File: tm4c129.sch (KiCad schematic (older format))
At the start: 45 parts, among them SW401 RST_SW, U401 TM4C1294NCPDTGOOD, Y401 Crystal_GND24, Y402 Crystal

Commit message: replaced battery with ldo connected to external vbatt. Layout passes DRC
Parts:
- removed BT401: Battery_Cell, Battery:BatteryHolder_Keystone_1058_1x2032, symbol Device:Battery_Cell
- added C1: 0.1u, Capacitor_SMD:C_0603_1608Metric, symbol Device:C_Small
- added C2: 10u, Capacitor_SMD:C_0603_1608Metric, symbol Device:C_Small
- added R1: 0, Capacitor_SMD:C_0603_1608Metric, symbol Device:R_Small
- added R2: DNP, Capacitor_SMD:C_0603_1608Metric, symbol Device:R_Small
- added U1: LT1761-3, Package_TO_SOT_SMD:TSOT-23-5, symbol Regulator_Linear:LT1761-3
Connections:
- net labels added: +BATT, VBat_R
- wire segments 249 -> 261
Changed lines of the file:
@@
 	5900 900  5900 1050
-$Comp
-L Device:Battery_Cell BT401
-U 1 1 5D11D2E9
-P 1450 1300
-F 0 "BT401" H 1568 1396 50  0000 L CNN
-F 1 "Battery_Cell" H 1568 1305 50  0000 L CNN
-F 2 "Battery:BatteryHolder_Keystone_1058_1x2032" V 1450 1360 50  0001 C CNN
-F 3 "~" V 1450 1360 50  0001 C CNN
-	1    1450 1300
-	1    0    0    -1
-$EndComp
-Wire Wire Line
-	1450 1100 1450 1050
-Wire Wire Line
-	1450 1050 1850 1050
 $Comp
 L Device:R_Small R401
@@
 Wire Wire Line
 	2150 1050 2150 1150
-Text Label 2400 1050 0    50   ~ 0
-VBat
+Text Label 2550 1050 0    50   ~ 0
+VBat_R
 Text Label 1450 1050 0    50   ~ 0
 Batt_Pos
@@
 L power:GND #PWR0405
 U 1 1 5D116091
-P 1450 1500
-F 0 "#PWR0405" H 1450 1250 50  0001 C CNN
-F 1 "GND" H 1455 1327 50  0000 C CNN
-F 2 "" H 1450 1500 50  0001 C CNN
-F 3 "" H 1450 1500 50  0001 C CNN
-	1    1450 1500
+P 2150 1500
+F 0 "#PWR0405" H 2150 1250 50  0001 C CNN
+F 1 "GND" H 2155 1327 50  0000 C CNN
+F 2 "" H 2150 1500 50  0001 C CNN
+F 3 "" H 2150 1500 50  0001 C CNN
+	1    2150 1500
 	1    0    0    -1
 $EndComp
@@
 $EndComp
 Wire Wire Line
-	1450 1400 1450 1450
-Wire Wire Line
-	1450 1450 2150 1450
-Wire Wire Line
-	2150 1450 2150 1350
-Wire Wire Line
-	1450 1500 1450 1450
-Connection ~ 1450 1450
-Wire Wire Line
 	5900 1150 5900 1300
-Wire Wire Line
-	2750 1050 2150 1050
-Connection ~ 2150 1050
 $Comp
 L Device:R_Small R407
@@
 Wire Wire Line
 	2600 2600 2600 2650
+Connection ~ 2600 2650
+Wire Wire Line
+	2450 2550 2450 2850
+Wire Wire Line
+	2150 1350 2150 1500
+$Comp
+L Regulator_Linear:LT1761-3 U1
+U 1 1 5D319EB9
+P 1050 1150
+F 0 "U1" H 1050 1517 50  0000 C CNN
+F 1 "LT1761-3" H 1050 1426 50  0000 C CNN
+F 2 "Package_TO_SOT_SMD:TSOT-23-5" H 1050 1475 50  0001 C CNN
+F 3 "https://www.analog.com/media/en/technical-documentation/data-sheets/1761sff.pdf" H 1050 1150 50  0001 C CNN
+	1    1050 1150
+	1    0    0    -1
+$EndComp
+Wire Wire Line
+	650  1050 600  1050
+Wire Wire Line
+	600  1050 600  1150
+Wire Wire Line
+	600  1150 650  1150
+Wire Wire Line
+	600  1050 600  950
+Connection ~ 600  1050
+$Comp
+L power:+BATT #PWR0101
+U 1 1 5D39C749
+P 600 950
+F 0 "#PWR0101" H 600 800 50  0001 C CNN
+F 1 "+BATT" H 615 1123 50  0000 C CNN
+F 2 "" H 600 950 50  0001 C CNN
+F 3 "" H 600 950 50  0001 C CNN
+	1    600  950
+	1    0    0    -1
+$EndComp
+Wire Wire Line
+	1050 1450 1050 1500
+$Comp
+L power:GND #PWR0102
+U 1 1 5D3B002F
+P 1050 1500
+F 0 "#PWR0102" H 1050 1250 50  0001 C CNN
+F 1 "GND" H 1055 1327 50  0000 C CNN
+F 2 "" H 1050 1500 50  0001 C CNN
+F 3 "" H 1050 1500 50  0001 C CNN
+	1    1050 1500
+	1    0    0    -1
+$EndComp
+$Comp
+L Device:C_Small C2
+U 1 1 5D3B0A26
+P 1800 1150
+F 0 "C2" H 1892 1196 50  0000 L CNN
+F 1 "10u" H 1892 1105 50  0000 L CNN
+F 2 "Capacitor_SMD:C_0603_1608Metric" H 1800 1150 50  0001 C CNN
+F 3 "~" H 1800 1150 50  0001 C CNN
+	1    1800 1150
+	1    0    0    -1
+$EndComp
+Wire Wire Line
+	1800 1250 1800 1300
+$Comp
+L power:GND #PWR0103
+U 1 1 5D3C4347
+P 1800 1300
+F 0 "#PWR0103" H 1800 1050 50  0001 C CNN
+F 1 "GND" H 1805 1127 50  0000 C CNN
+F 2 "" H 1800 1300 50  0001 C CNN
+F 3 "" H 1800 1300 50  0001 C CNN
+	1    1800 1300
+	1    0    0    -1
+$EndComp
+$Comp
+L Device:C_Small C1
+U 1 1 5D3E9FEA
+P 1600 1150
+F 0 "C1" H 1692 1196 50  0000 L CNN
+F 1 "0.1u" H 1692 1105 50  0000 L CNN
+F 2 "Capacitor_SMD:C_0603_1608Metric" H 1600 1150 50  0001 C CNN
+F 3 "~" H 1600 1150 50  0001 C CNN
+	1    1600 1150
+	1    0    0    -1
+$EndComp
+Connection ~ 1800 1050
+Wire Wire Line
+	1800 1050 1850 1050
+Wire Wire Line
+	1450 1050 1600 1050
+Connection ~ 1600 1050
+Wire Wire Line
+	1600 1050 1800 1050
+Wire Wire Line
+	1450 1150 1500 1150
+Wire Wire Line
+	1500 1300 1600 1300
+Wire Wire Line
+	1600 1300 1600 1250
+Wire Wire Line
+	1500 1150 1500 1300
+$Comp
+L Device:R_Small R1
+U 1 1 5D4424D9
+P 2300 1050
+F 0 "R1" V 2104 1050 50  0000 C CNN
+F 1 "0" V 2195 1050 50  0000 C CNN
+F 2 "Capacitor_SMD:C_0603_1608Metric" H 2300 1050 50  0001 C CNN
+F 3 "~" H 2300 1050 50  0001 C CNN
+	1    2300 1050
+	0    1    1    0
+$EndComp
+Text Label 2100 1050 0    50   ~ 0
+VBat
+Wire Wire Line
+	2200 1050 2150 1050
+Connection ~ 2150 1050
+Wire Wire Line
+	2400 1050 2500 1050
+$Comp
+L Device:R_Small R2
+U 1 1 5D4934F5
+P 2500 900
+F 0 "R2" H 2441 854 50  0000 R CNN
+F 1 "DNP" H 2441 945 50  0000 R CNN
+F 2 "Capacitor_SMD:C_0603_1608Metric" H 2500 900 50  0001 C CNN
+F 3 "~" H 2500 900 50  0001 C CNN
+	1    2500 900
+	-1   0    0    1
+$EndComp
+Wire Wire Line
+	2500 1000 2500 1050
+Connection ~ 2500 1050
+Wire Wire Line
+	2500 1050 2750 1050
+$Comp
+L power:+3.3V #PWR0104
+U 1 1 5D4A8C01
+P 2500 750
+F 0 "#PWR0104" H 2500 600 50  0001 C CNN
+F 1 "+3.3V" H 2515 923 50  0000 C CNN
+F 2 "" H 2500 750 50  0001 C CNN
+F 3 "" H 2500 750 50  0001 C CNN
+	1    2500 750
+	1    0    0    -1
+$EndComp
+Wire Wire Line
+	2500 750  2500 800
 Wire Bus Line
 	1700 4850 1700 7600
 Wire Bus Line
 	6000 2200 6000 7600
-Connection ~ 2600 2650
-Wire Wire Line
-	2450 2550 2450 2850
 $EndSCHEMATC

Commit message: moved ldo vbatt circuit to a sheet
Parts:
- removed C1: 0.1u, Capacitor_SMD:C_0603_1608Metric, symbol Device:C_Small
- removed C2: 10u, Capacitor_SMD:C_0603_1608Metric, symbol Device:C_Small
- removed R401: 51, Resistor_SMD:R_0603_1608Metric, symbol Device:R_Small
- removed U1: LT1761-3, Package_TO_SOT_SMD:TSOT-23-5, symbol Regulator_Linear:LT1761-3
- added R3: 51, Resistor_SMD:R_0603_1608Metric, symbol Device:R_Small
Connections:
- net labels removed: +BATT, Batt_Pos
- wire segments 261 -> 249
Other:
- moved on the sheet: C410, R1, R2
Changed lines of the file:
@@
 $Descr A4 11693 8268
 encoding utf-8
-Sheet 4 5
+Sheet 4 6
 Title "TM4C129"
 Date "2019-06-22"
@@
 	5900 900  5900 1050
 $Comp
-L Device:R_Small R401
-U 1 1 5D132E60
-P 1950 1050
-F 0 "R401" V 1754 1050 50  0000 C CNN
-F 1 "51" V 1845 1050 50  0000 C CNN
-F 2 "Resistor_SMD:R_0603_1608Metric" H 1950 1050 50  0001 C CNN
-F 3 "~" H 1950 1050 50  0001 C CNN
-	1    1950 1050
-	0    1    1    0
-$EndComp
-$Comp
 L Device:C_Small C410
 U 1 1 5D1335F6
-P 2150 1250
-F 0 "C410" H 2242 1296 50  0000 L CNN
-F 1 "0.1u" H 2242 1205 50  0000 L CNN
-F 2 "Capacitor_SMD:C_0603_1608Metric" H 2150 1250 50  0001 C CNN
-F 3 "~" H 2150 1250 50  0001 C CNN
-	1    2150 1250
-	1    0    0    -1
-$EndComp
-Wire Wire Line
-	2050 1050 2150 1050
-Wire Wire Line
-	2150 1050 2150 1150
-Text Label 2550 1050 0    50   ~ 0
+P 1650 1250
+F 0 "C410" H 1742 1296 50  0000 L CNN
+F 1 "0.1u" H 1742 1205 50  0000 L CNN
+F 2 "Capacitor_SMD:C_0603_1608Metric" H 1650 1250 50  0001 C CNN
+F 3 "~" H 1650 1250 50  0001 C CNN
+	1    1650 1250
+	1    0    0    -1
+$EndComp
+Wire Wire Line
+	1550 1050 1650 1050
+Wire Wire Line
+	1650 1050 1650 1150
+Text Label 2150 1050 0    50   ~ 0
 VBat_R
-Text Label 1450 1050 0    50   ~ 0
-Batt_Pos
 $Comp
 L Device:Crystal Y402
@@
 L power:GND #PWR0405
 U 1 1 5D116091
-P 2150 1500
-F 0 "#PWR0405" H 2150 1250 50  0001 C CNN
-F 1 "GND" H 2155 1327 50  0000 C CNN
-F 2 "" H 2150 1500 50  0001 C CNN
-F 3 "" H 2150 1500 50  0001 C CNN
-	1    2150 1500
+P 1650 1500
+F 0 "#PWR0405" H 1650 1250 50  0001 C CNN
+F 1 "GND" H 1655 1327 50  0000 C CNN
+F 2 "" H 1650 1500 50  0001 C CNN
+F 3 "" H 1650 1500 50  0001 C CNN
+	1    1650 1500
 	1    0    0    -1
 $EndComp
@@
 Text Notes 9500 650  0    50   ~ 0
 Bulk Cap should total 2.2uF to 22uF
-Text Notes 1050 800  0    50   ~ 0
-RC time circuit to meet ontime requirements
 Wire Bus Line
 	1700 4850 1550 4850
@@
 	2450 2550 2450 2850
 Wire Wire Line
-	2150 1350 2150 1500
-$Comp
-L Regulator_Linear:LT1761-3 U1
-U 1 1 5D319EB9
-P 1050 1150
-F 0 "U1" H 1050 1517 50  0000 C CNN
-F 1 "LT1761-3" H 1050 1426 50  0000 C CNN
-F 2 "Package_TO_SOT_SMD:TSOT-23-5" H 1050 1475 50  0001 C CNN
-F 3 "https://www.analog.com/media/en/technical-documentation/data-sheets/1761sff.pdf" H 1050 1150 50  0001 C CNN
-	1    1050 1150
-	1    0    0    -1
-$EndComp
-Wire Wire Line
-	650  1050 600  1050
-Wire Wire Line
-	600  1050 600  1150
-Wire Wire Line
-	600  1150 650  1150
-Wire Wire Line
-	600  1050 600  950
-Connection ~ 600  1050
-$Comp
-L power:+BATT #PWR0101
-U 1 1 5D39C749
-P 600 950
-F 0 "#PWR0101" H 600 800 50  0001 C CNN
-F 1 "+BATT" H 615 1123 50  0000 C CNN
-F 2 "" H 600 950 50  0001 C CNN
-F 3 "" H 600 950 50  0001 C CNN
-	1    600  950
-	1    0    0    -1
-$EndComp
-Wire Wire Line
-	1050 1450 1050 1500
-$Comp
-L power:GND #PWR0102
-U 1 1 5D3B002F
-P 1050 1500
-F 0 "#PWR0102" H 1050 1250 50  0001 C CNN
-F 1 "GND" H 1055 1327 50  0000 C CNN
-F 2 "" H 1050 1500 50  0001 C CNN
-F 3 "" H 1050 1500 50  0001 C CNN
-	1    1050 1500
-	1    0    0    -1
-$EndComp
-$Comp
-L Device:C_Small C2
-U 1 1 5D3B0A26
-P 1800 1150
-F 0 "C2" H 1892 1196 50  0000 L CNN
-F 1 "10u" H 1892 1105 50  0000 L CNN
-F 2 "Capacitor_SMD:C_0603_1608Metric" H 1800 1150 50  0001 C CNN
-F 3 "~" H 1800 1150 50  0001 C CNN
-	1    1800 1150
-	1    0    0    -1
-$EndComp
-Wire Wire Line
-	1800 1250 1800 1300
-$Comp
-L power:GND #PWR0103
-U 1 1 5D3C4347
-P 1800 1300
-F 0 "#PWR0103" H 1800 1050 50  0001 C CNN
-F 1 "GND" H 1805 1127 50  0000 C CNN
-F 2 "" H 1800 1300 50  0001 C CNN
-F 3 "" H 1800 1300 50  0001 C CNN
-	1    1800 1300
-	1    0    0    -1
-$EndComp
-$Comp
-L Device:C_Small C1
-U 1 1 5D3E9FEA
-P 1600 1150
-F 0 "C1" H 1692 1196 50  0000 L CNN
-F 1 "0.1u" H 1692 1105 50  0000 L CNN
-F 2 "Capacitor_SMD:C_0603_1608Metric" H 1600 1150 50  0001 C CNN
-F 3 "~" H 1600 1150 50  0001 C CNN
-	1    1600 1150
-	1    0    0    -1
-$EndComp
-Connection ~ 1800 1050
-Wire Wire Line
-	1800 1050 1850 1050
-Wire Wire Line
-	1450 1050 1600 1050
-Connection ~ 1600 1050
-Wire Wire Line
-	1600 1050 1800 1050
-Wire Wire Line
-	1450 1150 1500 1150
-Wire Wire Line
-	1500 1300 1600 1300
-Wire Wire Line
-	1600 1300 1600 1250
-Wire Wire Line
-	1500 1150 1500 1300
+	1650 1350 1650 1500
 $Comp
 L Device:R_Small R1
 U 1 1 5D4424D9
-P 2300 1050
-F 0 "R1" V 2104 1050 50  0000 C CNN
-F 1 "0" V 2195 1050 50  0000 C CNN
-F 2 "Capacitor_SMD:C_0603_1608Metric" H 2300 1050 50  0001 C CNN
-F 3 "~" H 2300 1050 50  0001 C CNN
-	1    2300 1050
+P 1900 1050
+F 0 "R1" V 1704 1050 50  0000 C CNN
+F 1 "0" V 1795 1050 50  0000 C CNN
+F 2 "Capacitor_SMD:C_0603_1608Metric" H 1900 1050 50  0001 C CNN
+F 3 "~" H 1900 1050 50  0001 C CNN
+	1    1900 1050
 	0    1    1    0
 $EndComp
-Text Label 2100 1050 0    50   ~ 0
+Text Label 1600 1050 0    50   ~ 0
 VBat
-Wire Wire Line
-	2200 1050 2150 1050
-Connection ~ 2150 1050
-Wire Wire Line
-	2400 1050 2500 1050
+Connection ~ 1650 1050
 $Comp
 L Device:R_Small R2
 U 1 1 5D4934F5
-P 2500 900
-F 0 "R2" H 2441 854 50  0000 R CNN
-F 1 "DNP" H 2441 945 50  0000 R CNN
-F 2 "Capacitor_SMD:C_0603_1608Metric" H 2500 900 50  0001 C CNN
-F 3 "~" H 2500 900 50  0001 C CNN
-	1    2500 900
+P 2550 850
+F 0 "R2" H 2491 804 50  0000 R CNN
+F 1 "DNP" H 2491 895 50  0000 R CNN
+F 2 "Capacitor_SMD:C_0603_1608Metric" H 2550 850 50  0001 C CNN
+F 3 "~" H 2550 850 50  0001 C CNN
+	1    2550 850
 	-1   0    0    1
 $EndComp
-Wire Wire Line
-	2500 1000 2500 1050
-Connection ~ 2500 1050
-Wire Wire Line
-	2500 1050 2750 1050
 $Comp
 L power:+3.3V #PWR0104
 U 1 1 5D4A8C01
-P 2500 750
-F 0 "#PWR0104" H 2500 600 50  0001 C CNN
-F 1 "+3.3V" H 2515 923 50  0000 C CNN
-F 2 "" H 2500 750 50  0001 C CNN
-F 3 "" H 2500 750 50  0001 C CNN
-	1    2500 750
-	1    0    0    -1
-$EndComp
-Wire Wire Line
-	2500 750  2500 800
+P 2550 700
+F 0 "#PWR0104" H 2550 550 50  0001 C CNN
+F 1 "+3.3V" H 2565 873 50  0000 C CNN
+F 2 "" H 2550 700 50  0001 C CNN
+F 3 "" H 2550 700 50  0001 C CNN
+	1    2550 700
+	1    0    0    -1
+$EndComp
+Wire Wire Line
+	2550 700  2550 750
+$Sheet
+S 700  950  550  200
+U 5D2CB049
+F0 "V_Batt" 50
+F1 "v_batt.sch" 50
+F2 "Vout" I R 1250 1050 50
+$EndSheet
+Text Notes 550  800  0    50   ~ 0
+RC time circuit to meet ontime requirements
+$Comp
+L Device:R_Small R3
+U 1 1 5D306A2C
+P 1450 1050
+AR Path="/5C80AE96/5D306A2C" Ref="R3"  Part="1"
+AR Path="/5C80AE96/5D2CB049/5D306A2C" Ref="R?"  Part="1"
+F 0 "R3" V 1254 1050 50  0000 C CNN
+F 1 "51" V 1345 1050 50  0000 C CNN
+F 2 "Resistor_SMD:R_0603_1608Metric" H 1450 1050 50  0001 C CNN
+F 3 "~" H 1450 1050 50  0001 C CNN
+	1    1450 1050
+	0    1    1    0
+$EndComp
+Wire Wire Line
+	1650 1050 1800 1050
+Wire Wire Line
+	1250 1050 1350 1050
+Wire Wire Line
+	2000 1050 2550 1050
+Wire Wire Line
+	2550 950  2550 1050
 Wire Bus Line
 	1700 4850 1700 7600
 Wire Bus Line
 	6000 2200 6000 7600
+Connection ~ 2550 1050
+Wire Wire Line
+	2550 1050 2750 1050
 $EndSCHEMATC

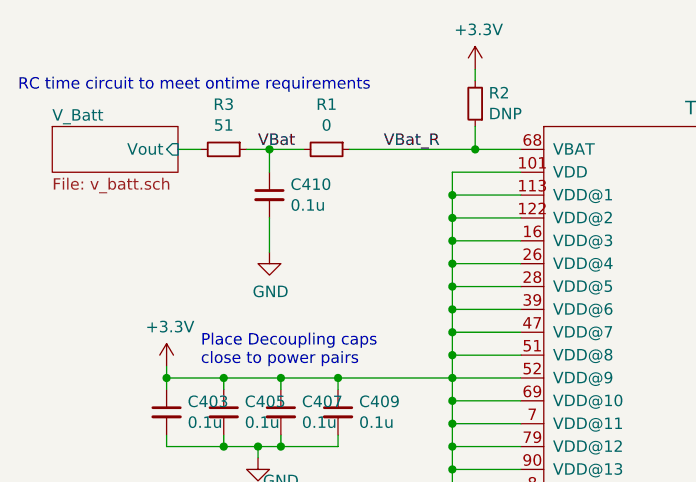
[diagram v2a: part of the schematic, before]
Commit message: removed rc filter on vbatt output. Included ltspice sim to prove it's unneeded.
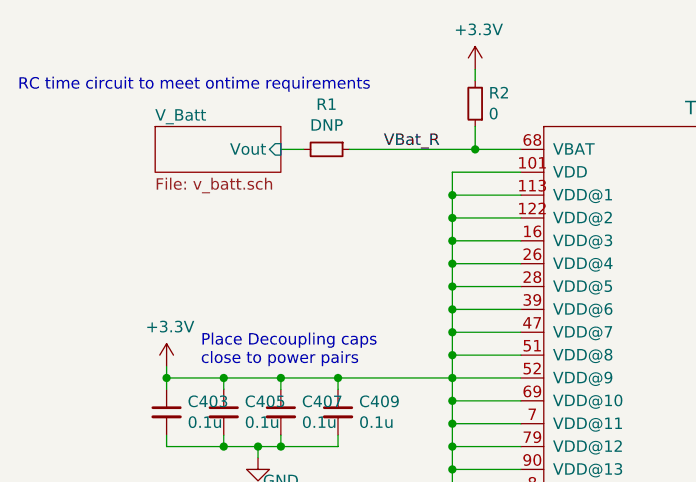
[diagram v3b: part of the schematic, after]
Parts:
- removed C410: 0.1u, Capacitor_SMD:C_0603_1608Metric, symbol Device:C_Small
- removed R3: 51, Resistor_SMD:R_0603_1608Metric, symbol Device:R_Small
- R1: value 0 -> DNP
- R2: value DNP -> 0
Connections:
- net labels removed: VBat
- wire segments 249 -> 245
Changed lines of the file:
@@
 Wire Wire Line
 	5900 900  5900 1050
-$Comp
-L Device:C_Small C410
-U 1 1 5D1335F6
-P 1650 1250
-F 0 "C410" H 1742 1296 50  0000 L CNN
-F 1 "0.1u" H 1742 1205 50  0000 L CNN
-F 2 "Capacitor_SMD:C_0603_1608Metric" H 1650 1250 50  0001 C CNN
-F 3 "~" H 1650 1250 50  0001 C CNN
-	1    1650 1250
-	1    0    0    -1
-$EndComp
-Wire Wire Line
-	1550 1050 1650 1050
-Wire Wire Line
-	1650 1050 1650 1150
 Text Label 2150 1050 0    50   ~ 0
 VBat_R
@@
 	1    6100 1100
 	0    1    -1   0
-$EndComp
-$Comp
-L power:GND #PWR0405
-U 1 1 5D116091
-P 1650 1500
-F 0 "#PWR0405" H 1650 1250 50  0001 C CNN
-F 1 "GND" H 1655 1327 50  0000 C CNN
-F 2 "" H 1650 1500 50  0001 C CNN
-F 3 "" H 1650 1500 50  0001 C CNN
-	1    1650 1500
-	1    0    0    -1
 $EndComp
 $Comp
@@
 Wire Wire Line
 	2450 2550 2450 2850
-Wire Wire Line
-	1650 1350 1650 1500
 $Comp
 L Device:R_Small R1
@@
 P 1900 1050
 F 0 "R1" V 1704 1050 50  0000 C CNN
-F 1 "0" V 1795 1050 50  0000 C CNN
+F 1 "DNP" V 1795 1050 50  0000 C CNN
 F 2 "Capacitor_SMD:C_0603_1608Metric" H 1900 1050 50  0001 C CNN
 F 3 "~" H 1900 1050 50  0001 C CNN
@@
 	0    1    1    0
 $EndComp
-Text Label 1600 1050 0    50   ~ 0
-VBat
-Connection ~ 1650 1050
 $Comp
 L Device:R_Small R2
@@
 P 2550 850
 F 0 "R2" H 2491 804 50  0000 R CNN
-F 1 "DNP" H 2491 895 50  0000 R CNN
+F 1 "0" H 2491 895 50  0000 R CNN
 F 2 "Capacitor_SMD:C_0603_1608Metric" H 2550 850 50  0001 C CNN
 F 3 "~" H 2550 850 50  0001 C CNN
@@
 	2550 700  2550 750
 $Sheet
-S 700  950  550  200
+S 1150 950  550  200
 U 5D2CB049
 F0 "V_Batt" 50
 F1 "v_batt.sch" 50
-F2 "Vout" I R 1250 1050 50
+F2 "Vout" I R 1700 1050 50
 $EndSheet
 Text Notes 550  800  0    50   ~ 0
 RC time circuit to meet ontime requirements
-$Comp
-L Device:R_Small R3
-U 1 1 5D306A2C
-P 1450 1050
-AR Path="/5C80AE96/5D306A2C" Ref="R3"  Part="1"
-AR Path="/5C80AE96/5D2CB049/5D306A2C" Ref="R?"  Part="1"
-F 0 "R3" V 1254 1050 50  0000 C CNN
-F 1 "51" V 1345 1050 50  0000 C CNN
-F 2 "Resistor_SMD:R_0603_1608Metric" H 1450 1050 50  0001 C CNN
-F 3 "~" H 1450 1050 50  0001 C CNN
-	1    1450 1050
-	0    1    1    0
-$EndComp
-Wire Wire Line
-	1650 1050 1800 1050
-Wire Wire Line
-	1250 1050 1350 1050
+Wire Wire Line
+	1700 1050 1800 1050
 Wire Wire Line
 	2000 1050 2550 1050
 Wire Wire Line
 	2550 950  2550 1050
+Connection ~ 2550 1050
+Wire Wire Line
+	2550 1050 2750 1050
 Wire Bus Line
 	1700 4850 1700 7600
 Wire Bus Line
 	6000 2200 6000 7600
-Connection ~ 2550 1050
-Wire Wire Line
-	2550 1050 2750 1050
 $EndSCHEMATC

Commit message: sourced all parts, except LEDs. added bom. fixed a few footprints/values.
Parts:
- R1, R2: footprint Capacitor_SMD:C_0603_1608Metric -> Resistor_SMD:R_0603_1608Metric
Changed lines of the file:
@@
 F 0 "R1" V 1704 1050 50  0000 C CNN
 F 1 "DNP" V 1795 1050 50  0000 C CNN
-F 2 "Capacitor_SMD:C_0603_1608Metric" H 1900 1050 50  0001 C CNN
+F 2 "Resistor_SMD:R_0603_1608Metric" H 1900 1050 50  0001 C CNN
 F 3 "~" H 1900 1050 50  0001 C CNN
 	1    1900 1050
@@
 F 0 "R2" H 2491 804 50  0000 R CNN
 F 1 "0" H 2491 895 50  0000 R CNN
-F 2 "Capacitor_SMD:C_0603_1608Metric" H 2550 850 50  0001 C CNN
+F 2 "Resistor_SMD:R_0603_1608Metric" H 2550 850 50  0001 C CNN
 F 3 "~" H 2550 850 50  0001 C CNN
 	1    2550 850

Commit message: layout and schematic cleanup.
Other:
- note removed: "RC time circuit to meet ontime requirements"
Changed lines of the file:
@@
 F2 "Vout" I R 1700 1050 50
 $EndSheet
-Text Notes 550  800  0    50   ~ 0
-RC time circuit to meet ontime requirements
 Wire Wire Line
 	1700 1050 1800 1050
